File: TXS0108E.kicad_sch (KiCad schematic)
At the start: 14 parts, among them J23 TP_VCC, Q10 FDN306P, Q11 FDN306P, Q9 2N7002

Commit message: Update KiCad schematics/PCB and project files
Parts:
- added C38: 100nf, Capacitor_SMD:C_0805_2012Metric, symbol Device:C
- added U7: (no value), kiC:FMINI_PB_6X6, symbol MINI_PB_6X6:MINI_PB_6X6
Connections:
- net +3V3: now also U7.1 (P1), U7.2 (P2), U7.3 (P3)
- net +5V: now also C38.2, U7.4 (P4), U7.5 (P5), U7.6 (P6)
- net GND: now also C38.1, U7.10 (P10), U7.11 (P11), U7.12 (P12), U7.7 (P7), U7.8 (P8), U7.9 (P9)
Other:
- moved on the sheet: C36, C37, C55, C56, D5, J23, JP5, JP6, Q10, Q11, Q9, R29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

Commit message: add files update
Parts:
- added C52: 100nf, Capacitor_SMD:C_0805_2012Metric, symbol Device:C
- added J11: tp, TestPoint:TestPoint_Pad_D1.5mm, symbol Connector:Conn_01x01_Pin
- added J22: Conn_01x05_Pin, Connector_PinHeader_1.00mm:PinHeader_1x06_P1.00mm_Vertical_SMD_Pin1Left, symbol Connector:Conn_01x05_Pin
- added R69: 10k, Resistor_SMD:R_0805_2012Metric, symbol Device:R
- added U11: PIC10F206-IOT, Package_TO_SOT_SMD:SOT-23-6, symbol MCU_Microchip_PIC10:PIC10F206-IOT
- R53, R68: footprint Resistor_SMD:R_0603_1608Metric -> Resistor_SMD:R_0805_2012Metric
- U7: now left out of the parts list
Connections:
- net +3V3: now also C52.1, J22.2 (Pin_2), R69.1, U11.5 (VDD)
- net CONTROL: now also J22.4 (Pin_4), U11.1 (GP0)
- net GND: now also C52.2, J22.3 (Pin_3), U11.2 (VSS)
- net A8 renamed GP2
- net GP2: now also J11.1 (Pin_1), U11.4 (GP2)
- new net ICSPCLK: J22.5 (Pin_5), U11.3 (GP1)
- new net mlcr_pic10f: J22.1 (Pin_1), R69.2, U11.6 (GP3)
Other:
- moved on the sheet: C36, C37

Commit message: Actualización de esquemas y PCB con datos LCSC y librerías JLC
- Añade propiedades LCSC a los símbolos de las hojas de esquema
- Actualiza las hojas TXS0108E, display, esp32_c6, ft232, inmp441,
  led_sw_gpio, max98357a, micro_sd, power_supply y el esquema raíz
- Reorganiza el PCB (footprints, jumpers y nets) y actualiza el proyecto
- Incluye las librerías locales JLCImport (símbolos, huellas y modelos 3D)
  y las entradas correspondientes en fp-lib-table y sym-lib-table
- Añade la documentación técnica en docs/ y el archivo de posiciones
  esp32_xiaozhi-all.pos
- Elimina los ZIP generados gebers.zip y production.zip
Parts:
- C36, C37, C38, C52, C55, C56: LCSC (none) -> C1525
- D5: LCSC (none) -> C34499
- J11, J22, J23, JP5, JP6: now left out of the parts list
- Q10, Q11: LCSC (none) -> C5236682
- Q9: LCSC (none) -> C8545
- R29: LCSC (none) -> C4190
- R53, R68, R69: LCSC C25744 -> C17414
- U11: LCSC (none) -> C220623
- U7: now not fitted
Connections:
- net CONTROL renamed ICSPDAT
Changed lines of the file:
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@@
 	(wire
 		(pts
-			(xy 45.72 116.84) (xy 46.99 116.84)
-		)
-		(stroke
-			(width 0)
-			(type default)
-		)
-	)
-	(wire
-		(pts
 			(xy 46.99 124.46) (xy 46.99 127)
 		)
@@
 		)
 	)
-	(label "CONTROL"
-		(at 156.21 120.65 0)
-		(effects
-			(font
-				(size 1.27 1.27)
-			)
-			(justify left bottom)
-		)
-	)
 	(label "GP2"
 		(at 147.32 62.23 0)
@@
 			)
 		)
-		(property "LCSC" "C25744"
+		(property "LCSC" "C17414"
 			(at 146.05 111.76 0)
 			(hide yes)
@@
 		(body_style 1)
 		(exclude_from_sim no)
-		(in_bom yes)
+		(in_bom no)
 		(on_board yes)
 		(in_pos_files yes)
@@
 			)
 		)
+		(property "LCSC" "C8545"
+			(at 182.88 120.65 0)
+			(hide yes)
+			(show_name no)
+			(do_not_autoplace no)
+			(effects
+				(font
+					(size 1.27 1.27)
+				)
+			)
+		)
 		(pin "2"
 		)
@@
 			)
 		)
+		(property "LCSC" "C1525"
+			(at 44.45 133.35 0)
+			(hide yes)
+			(show_name no)
+			(do_not_autoplace no)
+			(effects
+				(font
+					(size 1.27 1.27)
+				)
+			)
+		)
 		(pin "1"
 		)
@@
 			)
 		)
+		(property "LCSC" "C1525"
+			(at 71.12 66.04 0)
+			(hide yes)
+			(show_name no)
+			(do_not_autoplace no)
+			(effects
+				(font
+					(size 1.27 1.27)
+				)
+			)
+		)
 		(pin "1"
 		)
@@
 			)
 		)
+		(property "LCSC" "C220623"
+			(at 132.08 59.69 0)
+			(hide yes)
+			(show_name no)
+			(do_not_autoplace no)
+			(effects
+				(font
+					(size 1.27 1.27)
+				)
+			)
+		)
 		(pin "3"
 		)
@@
 		(body_style 1)
 		(exclude_from_sim no)
-		(in_bom yes)
+		(in_bom no)
 		(on_board yes)
 		(in_pos_files yes)
@@
 			)
 		)
-		(property "LCSC" "C25744"
+		(property "LCSC" "C17414"
 			(at 149.86 124.46 0)
 			(hide yes)
@@
 			)
 		)
+		(property "LCSC" "C1525"
+			(at 124.46 113.03 0)
+			(hide yes)
+			(show_name no)
+			(do_not_autoplace no)
+			(effects
+				(font
+					(size 1.27 1.27)
+				)
+			)
+		)
 		(pin "1"
 		)
@@
 			)
 		)
+		(property "LCSC" "C1525"
+			(at 209.55 115.57 0)
+			(hide yes)
+			(show_name no)
+			(do_not_autoplace no)
+			(effects
+				(font
+					(size 1.27 1.27)
+				)
+			)
+		)
 		(pin "1"
 		)
@@
 		(body_style 1)
 		(exclude_from_sim no)
-		(in_bom yes)
+		(in_bom no)
 		(on_board yes)
 		(in_pos_files yes)
@@
 		(body_style 1)
 		(exclude_from_sim no)
-		(in_bom yes)
+		(in_bom no)
 		(on_board yes)
 		(in_pos_files yes)
@@
 			)
 		)
+		(property "LCSC" "C34499"
+			(at 198.12 110.49 90)
+			(hide yes)
+			(show_name no)
+			(do_not_autoplace no)
+			(effects
+				(font
+					(size 1.27 1.27)
+				)
+			)
+		)
 		(pin "1"
 		)
@@
 			)
 		)
+		(property "LCSC" "C5236682"
+			(at 182.88 100.33 90)
+			(hide yes)
+			(show_name no)
+			(do_not_autoplace no)
+			(effects
+				(font
+					(size 1.27 1.27)
+				)
+			)
+		)
 		(pin "1"
 		)
@@
 		(body_style 1)
 		(exclude_from_sim no)
-		(in_bom yes)
+		(in_bom no)
 		(on_board yes)
 		(in_pos_files yes)
@@
 			)
 		)
+		(property "LCSC" "C1525"
+			(at 85.09 66.04 0)
+			(hide yes)
+			(show_name no)
+			(do_not_autoplace no)
+			(effects
+				(font
+					(size 1.27 1.27)
+				)
+			)
+		)
 		(pin "1"
 		)
@@
 			)
 		)
+		(property "LCSC" "C4190"
+			(at 198.12 121.92 0)
+			(hide yes)
+			(show_name no)
+			(do_not_autoplace no)
+			(effects
+				(font
+					(size 1.27 1.27)
+				)
+			)
+		)
 		(pin "1"
 		)
@@
 			)
 		)
+		(property "LCSC" "C1525"
+			(at 99.06 66.04 0)
+			(hide yes)
+			(show_name no)
+			(do_not_autoplace no)
+			(effects
+				(font
+					(size 1.27 1.27)
+				)
+			)
+		)
 		(pin "1"
 		)
@@
 		(on_board yes)
 		(in_pos_files no)
-		(dnp no)
+		(dnp yes)
 		(fields_autoplaced yes)
 		(property "Reference" "U7"
@@
 			)
 		)
-		(property "LCSC" "C25744"
+		(property "LCSC" "C17414"
 			(at 198.12 48.26 0)
 			(hide yes)
@@
 			)
 		)
+		(property "LCSC" "C5236682"
+			(at 158.75 106.68 0)
+			(hide yes)
+			(show_name no)
+			(do_not_autoplace no)
+			(effects
+				(font
+					(size 1.27 1.27)
+				)
+			)
+		)

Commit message: Actualización de esquemas, PCB y librerías
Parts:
- C36, C37, C38, C52, C55, C56: LCSC C1525 -> C28233
- D5: value LED -> white/yellow
- R29: LCSC C4190 -> C17520
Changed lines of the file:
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@@
 			)
 		)
-		(property "LCSC" "C1525"
+		(property "LCSC" "C28233"
 			(at 44.45 133.35 0)
 			(hide yes)
@@
 			)
 		)
-		(property "LCSC" "C1525"
+		(property "LCSC" "C28233"
 			(at 71.12 66.04 0)
 			(hide yes)
@@
 			)
 		)
-		(property "LCSC" "C1525"
+		(property "LCSC" "C28233"
 			(at 124.46 113.03 0)
 			(hide yes)
@@
 			)
 		)
-		(property "LCSC" "C1525"
+		(property "LCSC" "C28233"
 			(at 209.55 115.57 0)
 			(hide yes)
@@
 			)
 		)
-		(property "Value" "LED"
+		(property "Value" "white/yellow"
 			(at 201.93 113.3474 90)
 			(show_name no)
@@
 			)
 		)
-		(property "LCSC" "C1525"
+		(property "LCSC" "C28233"
 			(at 85.09 66.04 0)
 			(hide yes)
@@
 			)
 		)
-		(property "LCSC" "C4190"
+		(property "LCSC" "C17520"
 			(at 198.12 121.92 0)
 			(hide yes)
@@
 			)
 		)
-		(property "LCSC" "C1525"
+		(property "LCSC" "C28233"
 			(at 99.06 66.04 0)
 			(hide yes)

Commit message: actualizacion  de pcb logic , rpi
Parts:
- Q10, Q11: Package TO-236-3 ON -> (none)
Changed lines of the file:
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@@
-			)
-		)
-		(property "Package" "TO-236-3 ON"
-			(at 182.88 100.33 0)
-			(hide yes)
-			(show_name no)
-			(do_not_autoplace no)
-			(effects
-				(font
-					(size 1.27 1.27)
-				)
-				(justify bottom)
 			)
 		)
@@
 			(at 158.75 106.68 0)
 			(hide yes)
-			(show_name no)
-			(do_not_autoplace no)
-			(effects
-				(font
-					(size 1.27 1.27)
-				)
-				(justify bottom)
-			)
-		)
-		(property "Package" "TO-236-3 ON"
-			(at 158.75 106.68 0)
-			(hide yes)

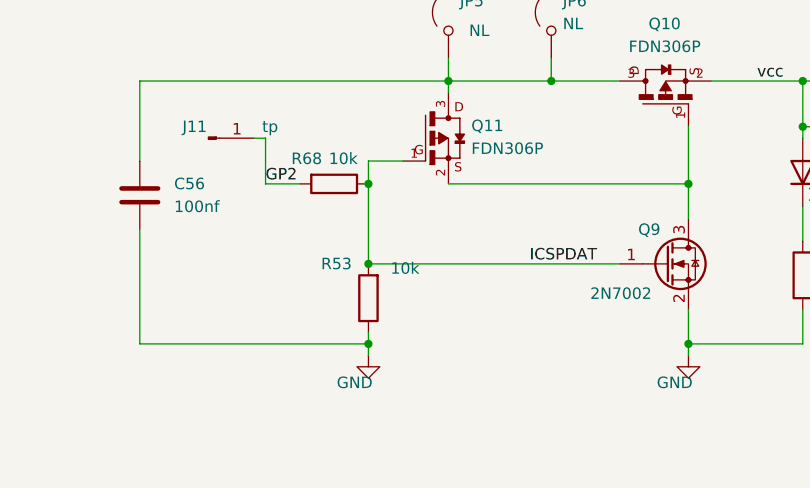
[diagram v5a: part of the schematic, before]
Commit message: correccion de numero de partes de componentes
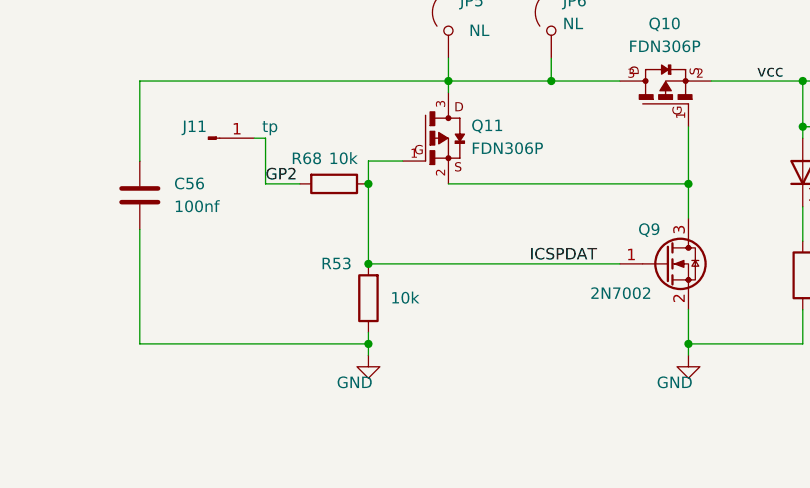
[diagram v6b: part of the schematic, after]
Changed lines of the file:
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@@
 		(in_bom no)
 		(on_board yes)
-		(in_pos_files yes)
+		(in_pos_files no)
 		(dnp no)
 		(fields_autoplaced yes)
@@
 		)
 		(property "Value" "10k"
-			(at 153.924 121.158 0)
+			(at 153.924 124.46 0)
 			(show_name no)
 			(do_not_autoplace no)
@@
 		(in_bom no)
 		(on_board yes)
-		(in_pos_files yes)
+		(in_pos_files no)
 		(dnp no)
 		(fields_autoplaced yes)
@@
 		(in_bom no)
 		(on_board yes)
-		(in_pos_files yes)
+		(in_pos_files no)
 		(dnp no)
 		(property "Reference" "J23"
@@
 		(in_bom no)
 		(on_board yes)
-		(in_pos_files yes)
+		(in_pos_files no)
 		(dnp no)
 		(property "Reference" "JP5"
